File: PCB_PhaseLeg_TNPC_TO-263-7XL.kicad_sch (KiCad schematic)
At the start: 4 parts, among them Q1 C3M0075120J, Q2 C3M0075120J, Q3 C3M0075120J, Q4 C3M0075120J

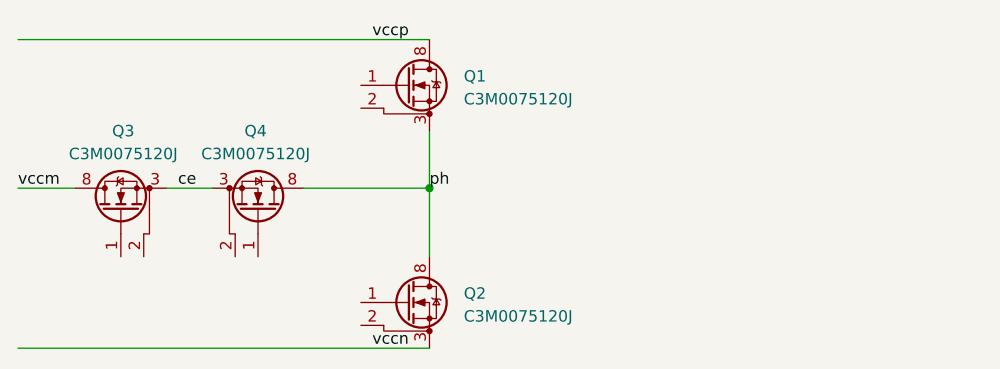
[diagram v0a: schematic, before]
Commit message: pcb heatsink
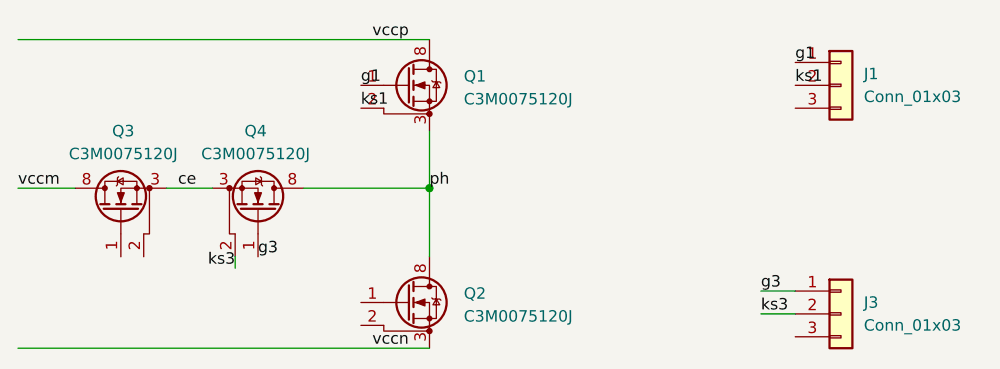
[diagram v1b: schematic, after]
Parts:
- added J1, J3: Conn_01x03, Connector_PinHeader_1.27mm:PinHeader_1x03_P1.27mm_Vertical_SMD_Pin1Left, symbol Connector_Generic:Conn_01x03
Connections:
- net g3: now reaches Q4.1 (G)
- net g3: now also J3.1 (Pin_1)
- net ks3: now reaches Q4.2 (DS)
- net ks3: now also J3.2 (Pin_2)
- net g1: now reaches Q1.1 (G)
- net g1: now also J1.1 (Pin_1)
- net ks1: now reaches Q1.2 (DS)
- net ks1: now also J1.2 (Pin_2)
